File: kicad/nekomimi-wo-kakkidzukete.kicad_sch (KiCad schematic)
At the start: 13 parts, among them J1 Conn_01x03_Pin, J2 Conn_01x03_Pin, J3 Conn_01x03_Pin, J4 Conn_01x03_Pin, J5 Conn_01x03_Pin, J6 Conn_01x03_Pin, U1 LM317_SOT-223, U2 ESP-12E

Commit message: something with kicad mb and readme
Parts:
- removed U1: LM317_SOT-223, Package_TO_SOT_SMD:SOT-223-3_TabPin2, symbol Regulator_Linear:LM317_SOT-223
- added R4: 340, symbol Device:R
- added U1, U3: AMS1117-3.3, Package_TO_SOT_SMD:SOT-223-3_TabPin2, symbol Regulator_Linear:AMS1117-3.3
- C1: value C -> 1uF
- C2: value C -> 10uF
- R1: value 200 -> 100
- R2: value 330 -> 100
- R3: value 10 -> 200
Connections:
- net GND: now also R4.2; no longer R3.2
- net +3.3V: now reaches R2.2, R3.1
- net +3.3V: now also C2.1, R1.2
- net at R2.1: now also U3.2 (VO); no longer R1.2
- net at R1.1: now also U1.2 (VO); no longer C2.1
- net +5V: now reaches C1.1
- net +5V: now also U1.3 (VI), U3.3 (VI)
- new net: R3.2, R4.1, U1.1 (GND), U3.1 (GND)

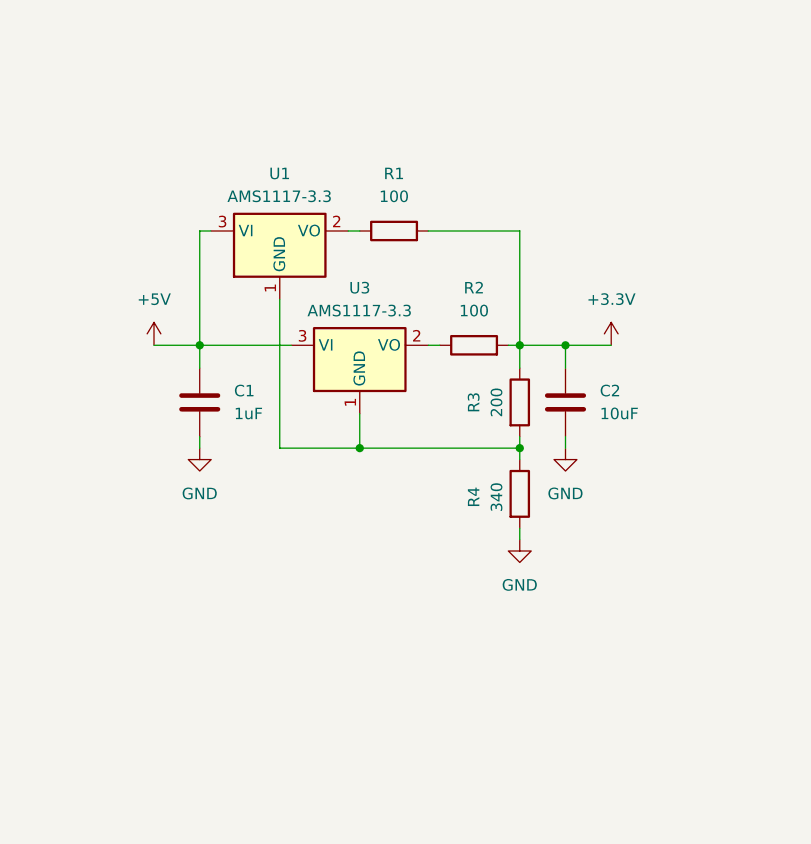
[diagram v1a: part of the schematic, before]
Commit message: better way of handling 2 voltage regulators
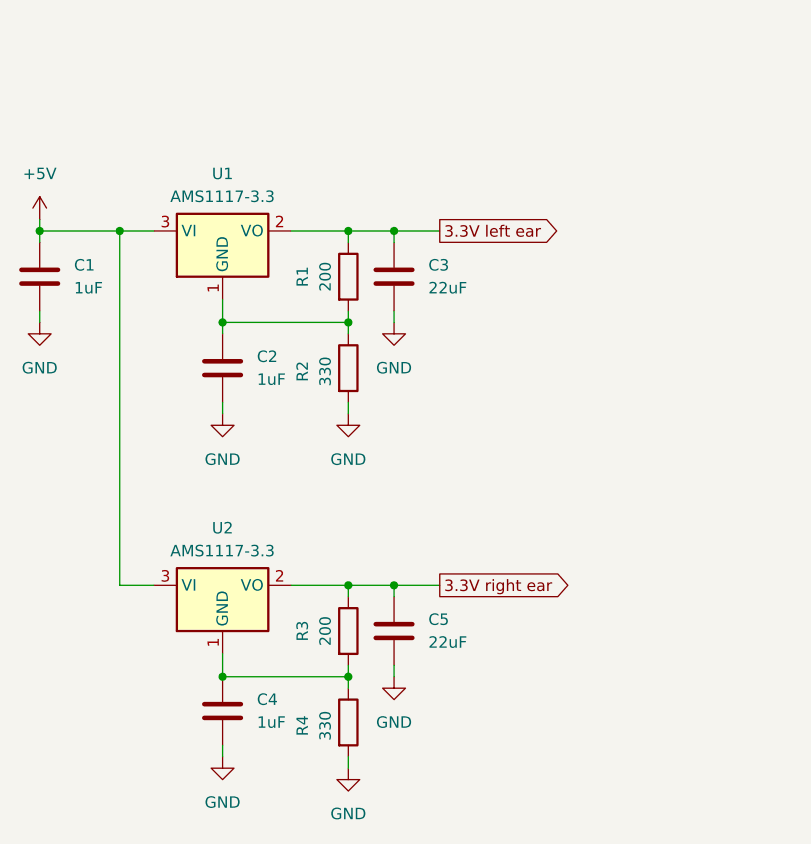
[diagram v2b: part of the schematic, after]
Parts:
- added C2, C4: 1uF, symbol Device:C
- added C3: 22uF, symbol Device:C
- C5: renamed from C2; value 10uF -> 22uF
- R1: value 100 -> 200
- R2: value 100 -> 330
- R4: value 340 -> 330
- renumbered U3 to U1, U1 to U2
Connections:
- net GND: now also R2.2, C2.2, C3.2, C4.2
- net 3.3V left ear: now reaches R1.1
- net 3.3V left ear: now also U1.2 (VO), C3.1; no longer U2.2 (VO)
- net at R3.2, R4.1, U2.1 (GND): now also C4.1; no longer U1.1 (GND)
- net at R2.1: now also R1.2, U1.1 (GND), C2.1; no longer U1.2 (VO)
- net +3.3V renamed 3.3V right ear
- net 3.3V right ear: now also U2.2 (VO); no longer R1.2, R2.2
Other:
- moved on the sheet: C1, C5, R3, R4, U1, U2
